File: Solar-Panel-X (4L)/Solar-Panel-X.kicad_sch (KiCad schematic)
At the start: 73 parts, among them J1 FTS-105-01-L-DV-A, Q1 BSS138DWQ-7, Q2 MBT2222ADW1T1, Q3 BSS138DWQ-7, Q4 MBT2222ADW1T1, U1 BQ25570RGRR, U2 TSL2561

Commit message: Changed TSL2591 to BH1750
All boards (4L) except -Y
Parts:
- removed U2: TSL2561, solarpanels:TSL2561, symbol solarpanels:symbols_TSL2561
- added U2: BH1750FVI-TR, WSOF6, symbol solarpanels:BH1750FVI-TR
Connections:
- net +3V3: now also U2.1 (VCC)
- net GND: now also U2.3 (GND)
- net SCL_LS: now also U2.6 (SCL)
- net SDA_LS: now also U2.4 (SDA)
- net at R10.2, R5.2, R7.2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: now also R5.1, R6.2, U1.7 (VBAT_OV)
- net at R1.1, R2.2: now also U2.2 (ADDR)
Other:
- moved on the sheet: C2, C3, C6, D1, D5, H1, H2, H3, H4, J1, R3, R4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

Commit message: Updated light sensor to OPT 3001, Updated solar diodes.
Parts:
- removed C12, C13: 10nF, Capacitor_SMD:C_0603_1608Metric, symbol Device:C
- removed D5: MSS1P4-M3_89A, solarpanels:MICROSMP, symbol Device:D_Schottky
- removed Q1, Q3: BSS138DWQ-7, Package_TO_SOT_SMD:SOT-363_SC-70-6, symbol mainboard:BSS138DWQ-7
- removed Q2, Q4: MBT2222ADW1T1, Package_TO_SOT_SMD:SOT-363_SC-70-6, symbol Transistor_BJT:MBT2222ADW1T1
- removed R19, R20: DNI, Resistor_SMD:R_0603_1608Metric, symbol Device:R_US
- removed R21, R26: 680, Resistor_SMD:R_0603_1608Metric, symbol Device:R_US
- removed R22, R27: 100K, Resistor_SMD:R_0603_1608Metric, symbol Device:R_US
- removed R23, R24, R28, R29: 10K, Resistor_SMD:R_0603_1608Metric, symbol Device:R_US
- removed R25, R30: 200K, Resistor_SMD:R_0603_1608Metric, symbol Device:R_US
- removed U2: BH1750FVI-TR, WSOF6, symbol solarpanels:BH1750FVI-TR
- added U2: OPT3001, solarpanels:OPT3001, symbol solarpanels:OPT3001
- added U3: MAX40200AUK, Package_TO_SOT_SMD:SOT-23-5, symbol Analog_Switch:MAX40200AUK
- C1: value 1uF -> 0.1uF
- D2, D3, D4: value MSS1P4-M3_89A -> DFLS130L-7; footprint solarpanels:MICROSMP -> Diode_SMD:D_PowerDI-123; Allied Price/Stock https://www.alliedelec.com/general-semiconductor-vishay-mss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 -> (none); Allied_Number 70217632 -> (none); Manufacturer_Name Vishay -> (none); Manufacturer_Part_Number MSS1P4-M3/89A -> (none); Mouser Part Number 625-MSS1P4-M3 -> (none); Mouser Price/Stock https://www.mouser.com/Search/Refine.aspx?Keyword=625-MSS1P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 -> (none); RS Part Number 7103068P -> (none); RS Price/Stock http://uk.rs-online.com/web/p/products/7103068P -> (none)
- J1: value FTS-105-01-L-DV-A -> FTS-105-01-X-DV-A
- R1, R12, R13, R16, R17, R18, R2, R3, R4: value 0 -> 0R
- R14, R15: value DNI -> DNI (0R)
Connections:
- net +3V3: now also U2.1 (VDD), U3.5 (OUT); no longer D2.1 (K)
- net GND: now also U2.3 (GND), U2.7 (GND), U3.2 (GND)
- net SCL_LS: now also U2.4 (SCL)
- net SDA_LS: now also U2.6 (SDA)
- net VSOLAR: now also D2.1 (K)
- net VSOLAR_FULL: now also D2.2 (A)
- net at R10.2, R5.2, R7.2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: no longer R5.1, R6.2, U1.7 (VBAT_OV)
- net at R1.1, R2.2: now also U2.2 (ADDR)
- net at C10.1, C8.1, L2.2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: now also U3.1 (VDD), U3.3 (EN); no longer D2.2 (A)
- new net: R5.1, R6.2, U1.7 (VBAT_OV)
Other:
- added sheet Bus Protection (BusProtection.kicad_sch)
- note added: "Populate R1 for I2C addr 0x45, OR Populate R2 for I2C addr 0x44"
- note added: "To Mainboard"
- note removed: "I2C Bus Protection - Light Sensor"
- moved on the sheet: C1, C11, R1, R12, R13, R17, R18, R2, R7

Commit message: B3/02 Updates
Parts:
- H1, H2, H3, H4: footprint MountingHole:MountingHole_2.2mm_M2_DIN965_Pad -> solarpanels:MountingHole_2.2mm_M2_DIN965_Pad_TopBottom; now left out of the parts list
- TP1, TP2, TP3, TP4: now left out of the parts list
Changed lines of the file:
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@@
   (title_block
     (title "PyCubed Mini")
-    (date "2023-02-19")
-    (rev "B3/01")
+    (date "2023-04-12")
+    (rev "B3/02")
     (company "REx Lab Carnegie Mellon University")
     (comment 1 "Z.Manchester")
@@
   )
   (symbol (lib_id "Connector:TestPoint") (at 195.58 176.53 0) (unit 1)
-    (in_bom yes) (on_board yes) (dnp no)
+    (in_bom no) (on_board yes) (dnp no)
     (property "Reference" "TP1" (at 197.0532 173.5328 0)
       (effects (font (size 1.27 1.27)) (justify left))
@@
   )
   (symbol (lib_id "Connector:TestPoint") (at 201.93 176.53 0) (unit 1)
-    (in_bom yes) (on_board yes) (dnp no)
+    (in_bom no) (on_board yes) (dnp no)
     (property "Reference" "TP2" (at 203.4032 173.5328 0)
       (effects (font (size 1.27 1.27)) (justify left))
@@
   )
   (symbol (lib_id "Connector:TestPoint") (at 208.28 176.53 0) (unit 1)
-    (in_bom yes) (on_board yes) (dnp no)
+    (in_bom no) (on_board yes) (dnp no)
     (property "Reference" "TP3" (at 209.7532 173.5328 0)
       (effects (font (size 1.27 1.27)) (justify left))
@@
   )
   (symbol (lib_id "Connector:TestPoint") (at 214.63 176.53 0) (unit 1)
-    (in_bom yes) (on_board yes) (dnp no)
+    (in_bom no) (on_board yes) (dnp no)
     (property "Reference" "TP4" (at 216.1032 173.5328 0)
       (effects (font (size 1.27 1.27)) (justify left))
@@
   )
   (symbol (lib_id "Mechanical:MountingHole_Pad") (at 207.01 116.84 270) (unit 1)
-    (in_bom yes) (on_board yes) (dnp no)
+    (in_bom no) (on_board yes) (dnp no)
     (property "Reference" "H1" (at 211.455 115.824 90)
       (effects (font (size 1.27 1.27)) (justify left))
@@
       (effects (font (size 1.27 1.27)) (justify left))
     )
-    (property "Footprint" "MountingHole:MountingHole_2.2mm_M2_DIN965_Pad" (at 207.01 116.84 0)
+    (property "Footprint" "solarpanels:MountingHole_2.2mm_M2_DIN965_Pad_TopBottom" (at 207.01 116.84 0)
       (effects (font (size 1.27 1.27)) hide)
     )
@@
   )
   (symbol (lib_id "Mechanical:MountingHole_Pad") (at 207.01 129.54 270) (unit 1)
-    (in_bom yes) (on_board yes) (dnp no)
+    (in_bom no) (on_board yes) (dnp no)
     (property "Reference" "H3" (at 211.455 128.2669 90)
       (effects (font (size 1.27 1.27)) (justify left))
@@
       (effects (font (size 1.27 1.27)) (justify left))
     )
-    (property "Footprint" "MountingHole:MountingHole_2.2mm_M2_DIN965_Pad" (at 207.01 129.54 0)
+    (property "Footprint" "solarpanels:MountingHole_2.2mm_M2_DIN965_Pad_TopBottom" (at 207.01 129.54 0)
       (effects (font (size 1.27 1.27)) hide)
     )
@@
   )
   (symbol (lib_id "Mechanical:MountingHole_Pad") (at 207.01 123.19 270) (unit 1)
-    (in_bom yes) (on_board yes) (dnp no)
+    (in_bom no) (on_board yes) (dnp no)
     (property "Reference" "H2" (at 211.455 121.9169 90)
       (effects (font (size 1.27 1.27)) (justify left))
@@
       (effects (font (size 1.27 1.27)) (justify left))
     )
-    (property "Footprint" "MountingHole:MountingHole_2.2mm_M2_DIN965_Pad" (at 207.01 123.19 0)
+    (property "Footprint" "solarpanels:MountingHole_2.2mm_M2_DIN965_Pad_TopBottom" (at 207.01 123.19 0)
       (effects (font (size 1.27 1.27)) hide)
     )
@@
   )
   (symbol (lib_id "Mechanical:MountingHole_Pad") (at 207.01 135.89 270) (unit 1)
-    (in_bom yes) (on_board yes) (dnp no)
+    (in_bom no) (on_board yes) (dnp no)
     (property "Reference" "H4" (at 211.455 134.4899 90)
       (effects (font (size 1.27 1.27)) (justify left))
@@
       (effects (font (size 1.27 1.27)) (justify left))
     )
-    (property "Footprint" "MountingHole:MountingHole_2.2mm_M2_DIN965_Pad" (at 207.01 135.89 0)
-      (effects (font (size 1.27 1.27)) hide)
-    )
+    (property "Footprint" "solarpanels:MountingHole_2.2mm_M2_DIN965_Pad_TopBottom" (at 207.01 135.89 0)
+      (effects (font (size 1.27 1.27)) hide)
+    )

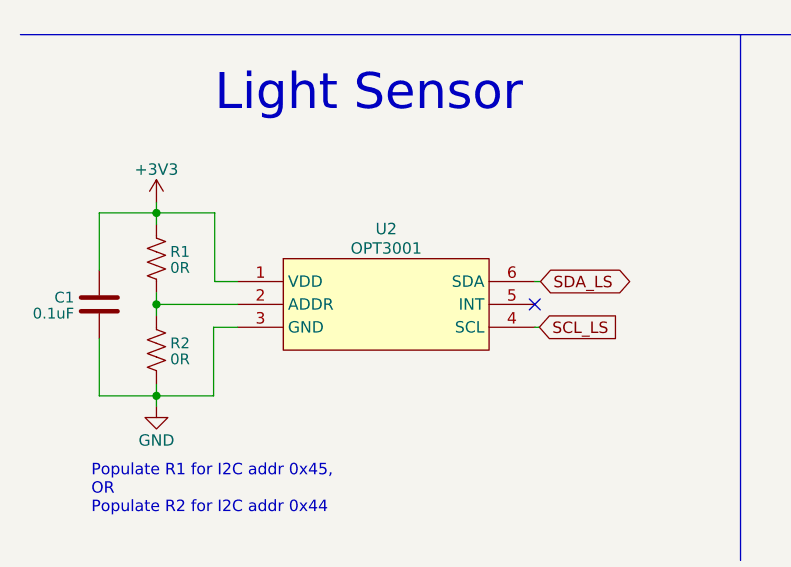
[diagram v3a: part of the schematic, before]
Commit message: Updated Sun Sensor to OPT4001
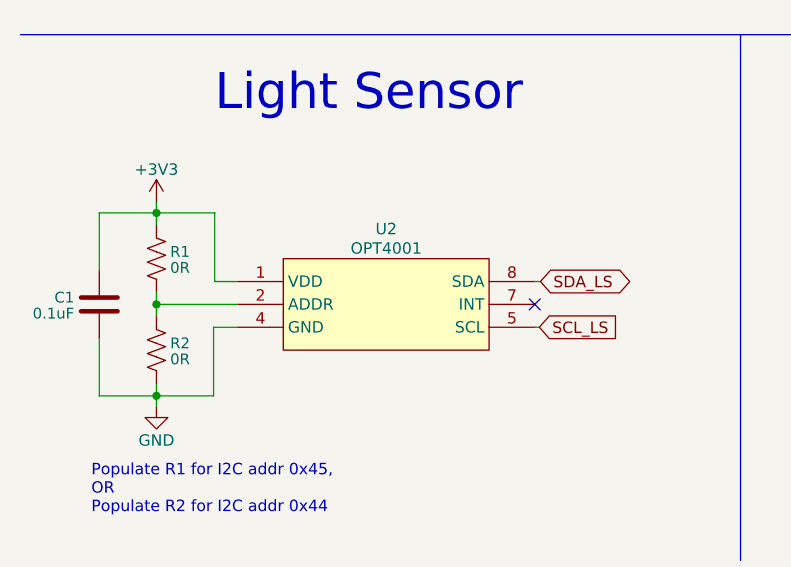
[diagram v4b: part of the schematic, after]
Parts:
- U2: value OPT3001 -> OPT4001; footprint solarpanels:OPT3001 -> Package_TO_SOT_SMD:SOT-583-8; symbol solarpanels:OPT3001 -> solarpanels:OPT4001
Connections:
- net GND: now also U2.4 (GND); no longer U2.3 (GND), U2.7 (GND)
- net SCL_LS: now also U2.5 (SCL); no longer U2.4 (SCL)
- net SDA_LS: now also U2.8 (SDA); no longer U2.6 (SDA)
- new net: U2.3 (NC), U2.6 (NC)
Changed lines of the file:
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@@
     )
   )
-  (symbol (lib_id "solarpanels:OPT3001") (at 52.07 176.022 0) (unit 1)
+  (symbol (lib_id "solarpanels:OPT4001") (at 52.07 176.022 0) (unit 1)
     (in_bom yes) (on_board yes) (dnp no)
     (property "Reference" "U2" (at 52.07 167.64 0)
       (effects (font (size 1.27 1.27)))
     )
-    (property "Value" "OPT3001" (at 52.07 169.799 0)
+    (property "Value" "OPT4001" (at 52.07 169.799 0)
       (effects (font (size 1.27 1.27)))
     )
-    (property "Footprint" "solarpanels:OPT3001" (at 52.07 182.372 0)
+    (property "Footprint" "Package_TO_SOT_SMD:SOT-583-8" (at 52.07 182.372 0)
       (effects (font (size 1.27 1.27)) hide)
     )
@@
     (pin "6")
     (pin "7")
+    (pin "8")
     (instances
       (project "Solar-Panel-X"
